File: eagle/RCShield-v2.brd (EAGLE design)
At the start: 92.7 x 82.5 mm, 48 parts, among them J1/J2 JOYSTICKPTH, U1 TOUSCRUINO_SHIELD, U2 FT232RL-BASICSSOP, U4 XBEE, X1 USBSMD

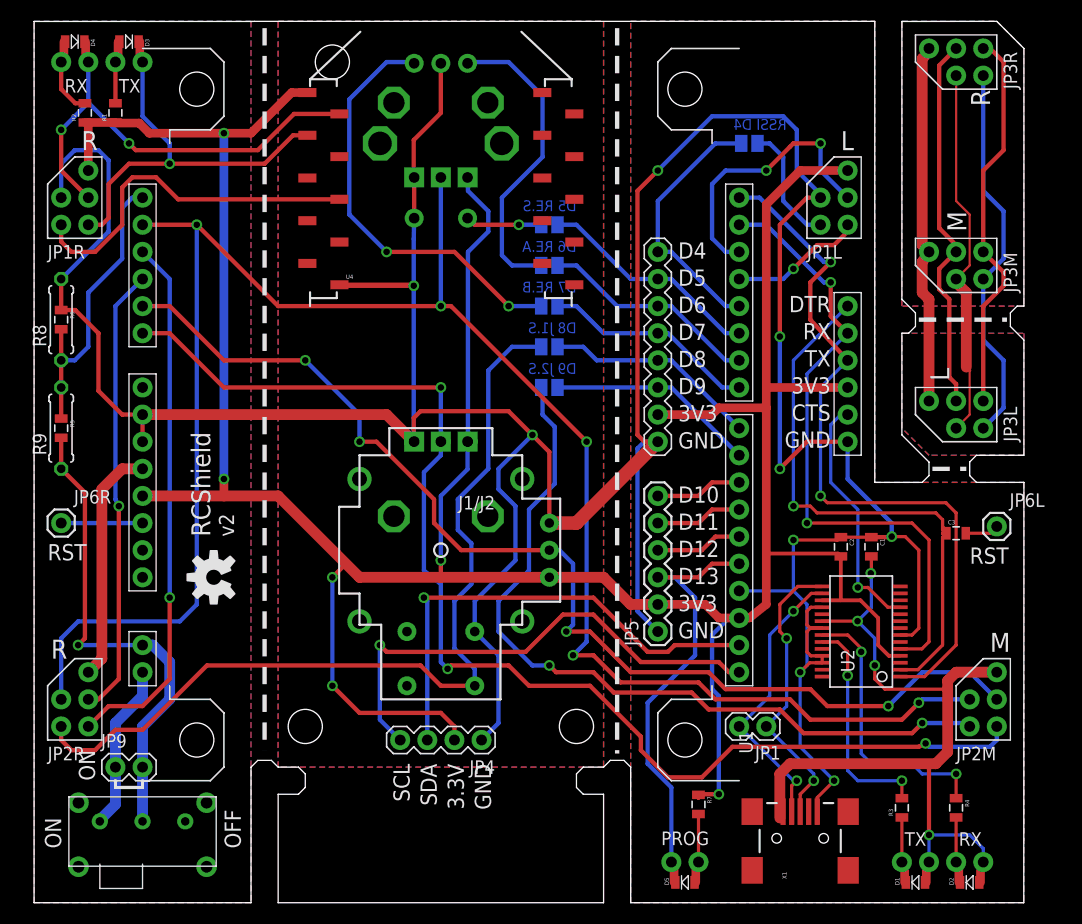
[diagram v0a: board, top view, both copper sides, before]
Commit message: 
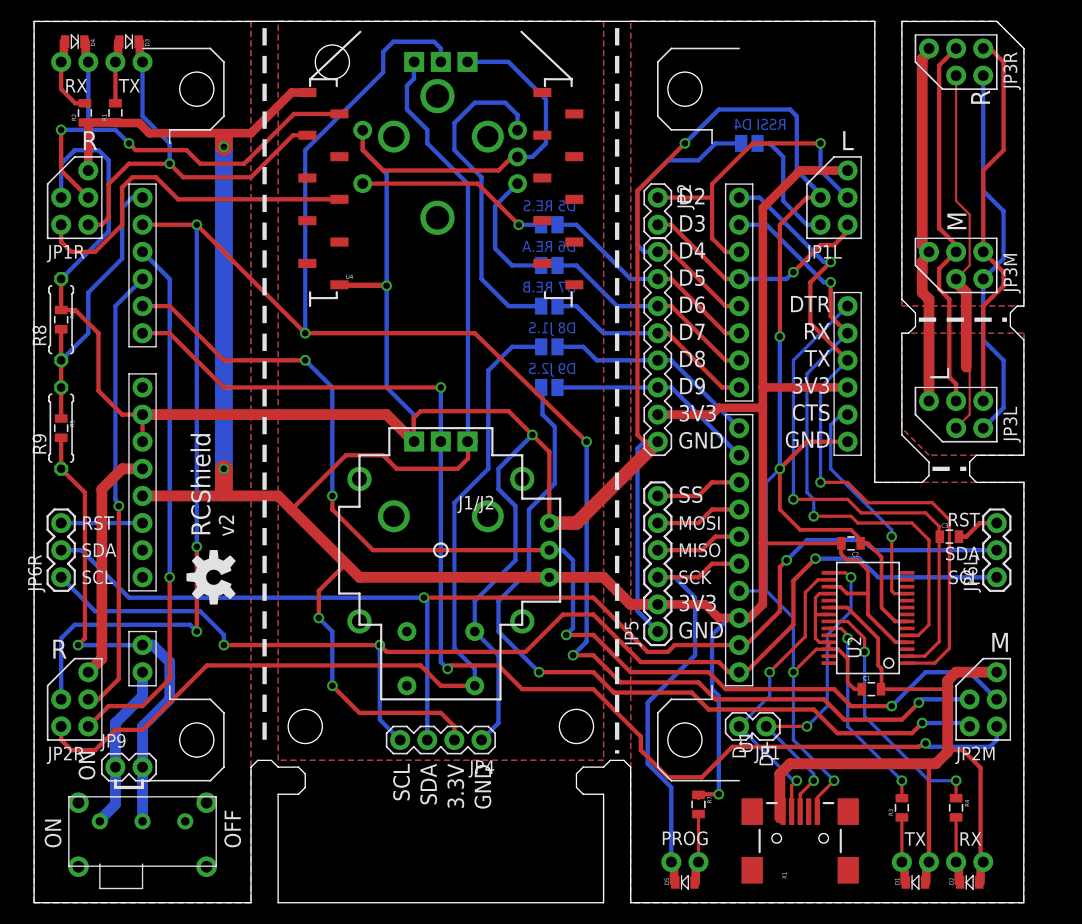
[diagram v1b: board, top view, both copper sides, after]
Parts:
- added JP2: UART1, wibauxl:1X02
- JP6L, JP6R: device SparkFun:1X01 -> SparkFun:1X03
- P1/P3, P2/P4: value (none) -> POT; device SparkFun:ALPS_POT -> wibauxl:ALPS_POT
- moved C1 13.3 mm to (78.4, 20.0), turned to 0 degrees
- moved JP6R 5.08 mm to (2.54, 30.5), turned to 90 degrees
- moved JP6L 4.76 mm to (90.2, 30.5), turned to 90 degrees
- moved P2/P4 3.18 mm to (38.1, 71.8), turned to 90 degrees
- moved U2 1.42 mm to (78.1, 26.7)
- moved RE1 1.31 mm to (37.8, 69.8), turned to 90 degrees
- moved C2 1.00 mm to (76.5, 33.7), turned to 180 degrees
- moved C3 0.71 mm to (85.7, 34.3)
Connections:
- removed net N$11: C3.2, JP6L.1
- new net N$1: C3.2, JP6L.3
- net RES: now also JP6R.3; no longer JP6R.1
- net RX1: now also JP2.1
- net SCL: now also JP6L.1, JP6R.1
- net SDA: now also JP6L.2, JP6R.2
- net TX1: now also JP2.2
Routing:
- net SDA: track 45.4 -> 112.1 mm, vias 1 -> 2
- net SCL: track 47.3 -> 112.0 mm, vias 1 -> 3
- net 3.3V: track 303.4 -> 334.8 mm, vias 6 -> 5
- net A4: track 178.3 -> 204.9 mm, vias 5 -> 7
- net GND: track 375.6 -> 401.7 mm, vias 9 -> 7
- net RE.A: track 29.0 -> 11.9 mm
- net RE.S: track 7.14 -> 18.3 mm
- net TX1: track 12.6 -> 22.4 mm
- net RE.B: track 39.9 -> 30.9 mm, vias 2 -> 0
- net RX1: track 26.0 -> 31.1 mm, vias 2 -> 1
- net D+: track 27.5 -> 32.0 mm, vias 2 -> 3
- net A1: track 105.3 -> 109.6 mm
- net N$1: track 0.00 -> 4.07 mm
- net U_DTR: track 53.4 -> 49.3 mm
- net D4: track 24.5 -> 28.5 mm
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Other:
- board text added: "D+"
- board text added: "D-"
- board text added: "D2"
- board text added: "D3"
- board text added: "MISO"
- board text added: "MOSI"
- board text added: "SCK"
- board text added: "SS"
- board text removed: "D10"
- board text removed: "D11"
- board text removed: "D12"
- board text removed: "D13"

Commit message: 
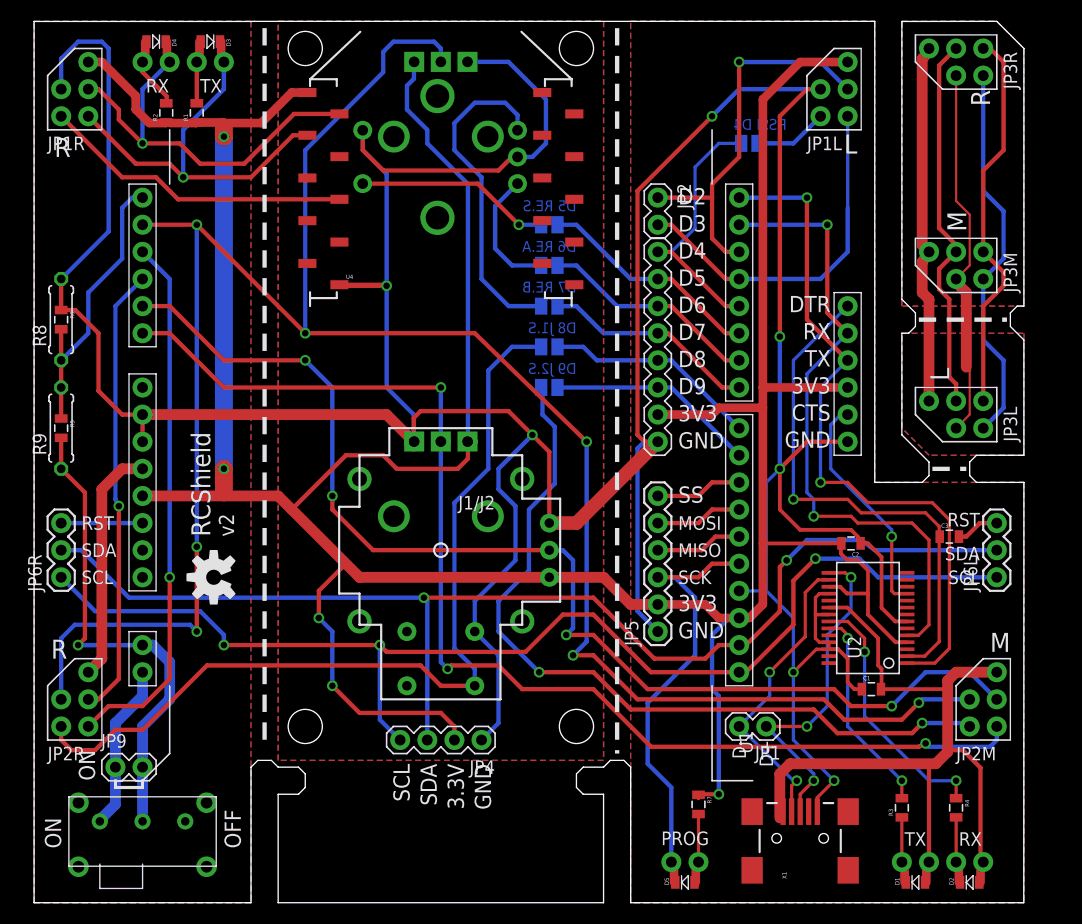
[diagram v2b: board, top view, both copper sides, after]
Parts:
- moved JP1L 10.2 mm to (73.7, 74.9)
- moved JP1R 10.2 mm to (2.54, 74.9)
- moved D3 7.62 mm to (16.5, 80.6)
- moved R1 7.62 mm to (15.2, 74.0)
- moved R2 7.62 mm to (12.4, 74.0)
- moved D4 7.62 mm to (11.4, 80.6)
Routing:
- net GND: track 401.7 -> 415.9 mm
- net TX1: track 22.4 -> 33.6 mm, vias 1 -> 0
- net 3.3V: track 334.8 -> 344.0 mm
- net RX1: track 31.1 -> 36.9 mm
- net X_TX: track 43.1 -> 37.6 mm, vias 2 -> 1
- net RSSI: track 33.8 -> 29.3 mm
- net _RSSI: track 11.5 -> 6.96 mm
- net D4: track 28.5 -> 25.1 mm
- net A0: track 116.2 -> 113.1 mm
- net U_RX: track 57.3 -> 60.3 mm
- net U_TX: track 65.1 -> 65.8 mm
- net X_RX: track 37.5 -> 36.9 mm
- net SDA: track 112.1 -> 112.6 mm
- net N$25: track 5.31 -> 4.81 mm

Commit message: 
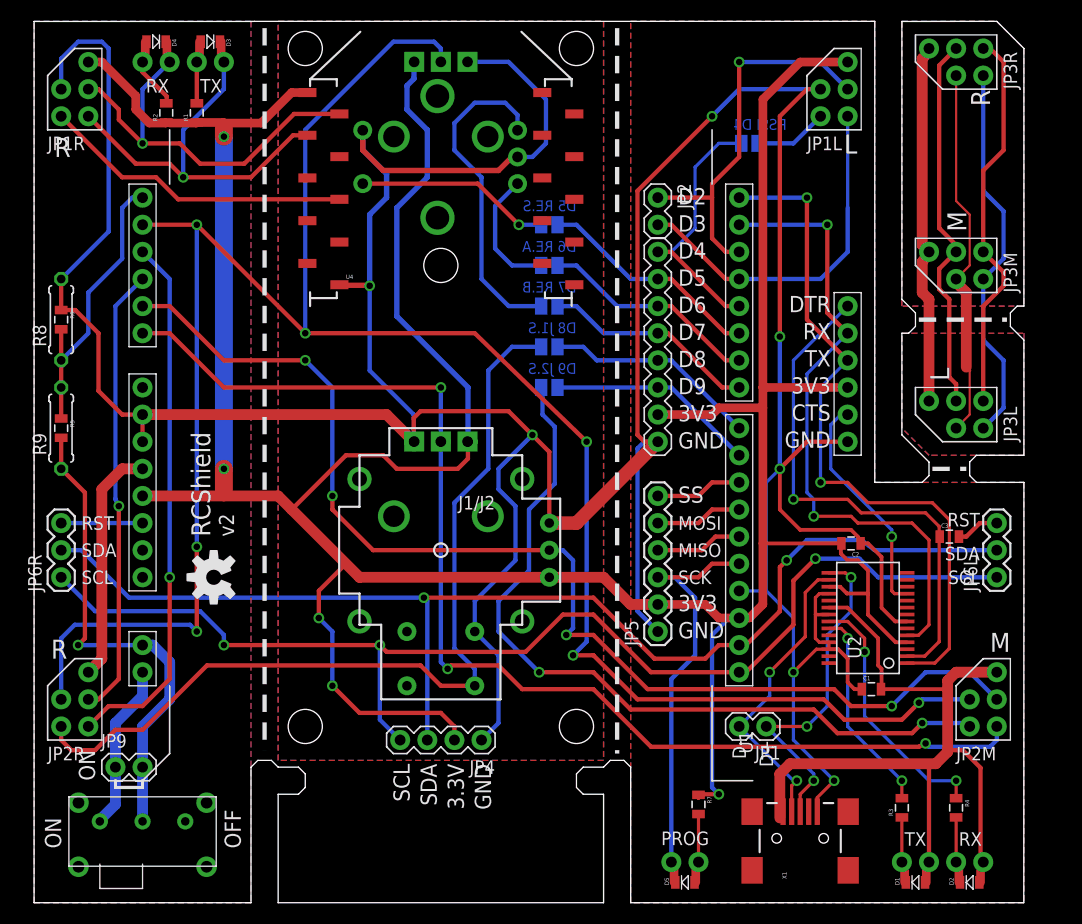
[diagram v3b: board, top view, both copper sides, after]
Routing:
- net 3.3V: track 344.0 -> 346.4 mm
- net GND: track 415.9 -> 414.0 mm
- net SCK: track 40.0 -> 38.1 mm
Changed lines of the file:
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@@
 <grid distance="12.5" unitdist="mil" unit="mil" style="lines" multiple="8" display="yes" altdistance="6.25" altunitdist="mil" altunit="mil"/>
 <layers>
-<layer number="1" name="Top" color="4" fill="1" visible="no" active="yes"/>
+<layer number="1" name="Top" color="4" fill="1" visible="yes" active="yes"/>
 <layer number="16" name="Bottom" color="1" fill="1" visible="yes" active="yes"/>
 <layer number="17" name="Pads" color="2" fill="1" visible="yes" active="yes"/>
@@
 <text x="60.325" y="65.405" size="1.524" layer="21" font="vector" ratio="15">D2</text>
 <hole x="50.8" y="80.01" drill="3.2"/>
+<hole x="38.1" y="59.69" drill="3.2"/>
 </plain>
 <attributes>
@@
 <wire x1="48.26" y1="35.56" x2="50.8" y2="35.56" width="1.27" layer="1"/>
 <wire x1="50.8" y1="35.56" x2="58.42" y2="43.18" width="1.27" layer="1"/>
-<wire x1="33.02" y1="57.785" x2="28.695" y2="57.785" width="0.4064" layer="1"/>
+<wire x1="31.4325" y1="57.785" x2="28.695" y2="57.785" width="0.4064" layer="1"/>
 <wire x1="28.695" y1="57.785" x2="28.6" y2="57.88" width="0.4064" layer="1"/>
 <wire x1="2.54" y1="76.2" x2="2.54" y2="79.0575" width="0.4064" layer="16"/>
@@
 <wire x1="6.985" y1="62.865" x2="2.54" y2="58.42" width="0.4064" layer="16"/>
 <wire x1="2.54" y1="55.51" x2="2.54" y2="58.42" width="0.4064" layer="1"/>
-<wire x1="28.6" y1="57.88" x2="32.925" y2="57.88" width="0.4064" layer="1"/>
-<wire x1="32.925" y1="57.88" x2="33.02" y2="57.785" width="0.4064" layer="1"/>
-<wire x1="33.02" y1="57.785" x2="33.02" y2="48.26" width="0.4064" layer="16"/>
+<wire x1="28.6" y1="57.88" x2="31.3375" y2="57.88" width="0.4064" layer="1"/>
+<wire x1="31.3375" y1="57.88" x2="31.4325" y2="57.785" width="0.4064" layer="1"/>
+<wire x1="31.4325" y1="57.785" x2="31.4325" y2="49.8475" width="0.4064" layer="16"/>
+<wire x1="31.4325" y1="49.8475" x2="33.02" y2="48.26" width="0.4064" layer="16"/>
 <wire x1="33.02" y1="48.26" x2="35.56" y2="45.72" width="0.4064" layer="16"/>
 <wire x1="35.56" y1="45.72" x2="35.56" y2="43.18" width="0.4064" layer="16"/>
-<via x="33.02" y="57.785" extent="1-16" drill="0.6096"/>
+<via x="31.4325" y="57.785" extent="1-16" drill="0.6096"/>
 <wire x1="35.56" y1="43.18" x2="33.02" y2="45.72" width="1.016" layer="1"/>
 <wire x1="33.02" y1="45.72" x2="10.16" y2="45.72" width="1.016" layer="1"/>
@@
 <vertex x="22.86" y="13.335"/>
 </polygon>
-<wire x1="30.7825" y1="72.35" x2="30.7825" y2="70.5" width="0.4064" layer="16"/>
-<wire x1="30.7825" y1="70.5" x2="33.02" y2="68.2625" width="0.4064" layer="16"/>
-<wire x1="33.02" y1="68.2625" x2="33.02" y2="57.785" width="0.4064" layer="16"/>
+<wire x1="30.7825" y1="72.35" x2="30.7825" y2="70.5" width="0.508" layer="16"/>
+<wire x1="30.7825" y1="70.5" x2="33.02" y2="68.2625" width="0.508" layer="16"/>
+<wire x1="33.02" y1="68.2625" x2="33.02" y2="66.04" width="0.508" layer="16"/>
+<wire x1="33.02" y1="66.04" x2="31.4325" y2="64.4525" width="0.508" layer="16"/>
+<wire x1="31.4325" y1="64.4525" x2="31.4325" y2="57.785" width="0.508" layer="16"/>
 <wire x1="45.2825" y1="69.85" x2="44.7675" y2="69.85" width="0.4064" layer="1"/>
-<wire x1="44.7675" y1="69.85" x2="43.4975" y2="68.58" width="0.4064" layer="1"/>
-<wire x1="43.4975" y1="68.58" x2="32.7025" y2="68.58" width="0.4064" layer="1"/>
-<wire x1="32.7025" y1="68.58" x2="30.7825" y2="70.5" width="0.4064" layer="1"/>
-<wire x1="30.7825" y1="70.5" x2="30.7825" y2="72.35" width="0.4064" layer="1"/>
+<wire x1="44.7675" y1="69.85" x2="43.4975" y2="68.58" width="0.508" layer="1"/>
+<wire x1="43.4975" y1="68.58" x2="32.7025" y2="68.58" width="0.508" layer="1"/>
+<wire x1="32.7025" y1="68.58" x2="30.7825" y2="70.5" width="0.508" layer="1"/>
+<wire x1="30.7825" y1="70.5" x2="30.7825" y2="72.35" width="0.508" layer="1"/>
 <wire x1="40.6" y1="78.755" x2="44.435" y2="78.755" width="0.4064" layer="16"/>
 <wire x1="44.435" y1="78.755" x2="47.9425" y2="75.2475" width="0.4064" layer="16"/>
@@
 <wire x1="66.04" y1="26.67" x2="65.0875" y2="26.67" width="0.4064" layer="16"/>
 <wire x1="65.0875" y1="26.67" x2="63.5" y2="25.0825" width="0.4064" layer="16"/>
-<wire x1="63.5" y1="25.0825" x2="63.5" y2="20.0025" width="0.4064" layer="16"/>
-<wire x1="63.5" y1="20.0025" x2="64.135" y2="19.3675" width="0.4064" layer="16"/>
-<wire x1="64.135" y1="19.3675" x2="64.135" y2="10.16" width="0.4064" layer="16"/>
+<wire x1="63.5" y1="25.0825" x2="63.5" y2="10.795" width="0.4064" layer="16"/>
+<wire x1="63.5" y1="10.795" x2="64.135" y2="10.16" width="0.4064" layer="16"/>
 <wire x1="64.135" y1="10.16" x2="62.5475" y2="10.16" width="0.4064" layer="1"/>
 <via x="64.135" y="10.16" extent="1-16" drill="0.6096"/>
@@
 <wire x1="17.78" y1="38.57625" x2="17.78" y2="38.1" width="0.3048" layer="1"/>
 <wire x1="17.78" y1="40.64" x2="17.78" y2="38.57625" width="1.6764" layer="1"/>
-<wire x1="35.6" y1="78.755" x2="35.575" y2="77.1675" width="0.4064" layer="16"/>
-<wire x1="35.575" y1="77.1675" x2="34.925" y2="76.5175" width="0.4064" layer="16"/>
-<wire x1="34.925" y1="76.5175" x2="34.925" y2="74.295" width="0.4064" layer="16"/>
-<wire x1="34.925" y1="74.295" x2="36.83" y2="72.39" width="0.4064" layer="16"/>
-<wire x1="36.83" y1="72.39" x2="36.83" y2="71.12" width="0.4064" layer="16"/>
-<wire x1="36.83" y1="71.12" x2="40.64" y2="67.31" width="0.4064" layer="16"/>
-<wire x1="40.64" y1="67.31" x2="40.64" y2="43.18" width="0.4064" layer="16"/>
+<wire x1="35.6" y1="78.755" x2="35.575" y2="77.1675" width="0.508" layer="16"/>
+<wire x1="35.575" y1="77.1675" x2="34.925" y2="76.5175" width="0.508" layer="16"/>
+<wire x1="34.925" y1="76.5175" x2="34.925" y2="74.295" width="0.508" layer="16"/>
+<wire x1="34.925" y1="74.295" x2="36.83" y2="72.39" width="0.508" layer="16"/>
+<wire x1="36.83" y1="72.39" x2="36.83" y2="67.945" width="0.508" layer="16"/>
+<wire x1="36.83" y1="67.945" x2="33.9725" y2="65.0875" width="0.508" layer="16"/>
+<wire x1="33.9725" y1="65.0875" x2="33.9725" y2="54.9275" width="0.508" layer="16"/>
+<wire x1="33.9725" y1="54.9275" x2="40.64" y2="48.26" width="0.508" layer="16"/>
+<wire x1="40.64" y1="48.26" x2="40.64" y2="43.18" width="0.508" layer="16"/>
 <wire x1="9.525" y1="74.295" x2="10.795" y2="73.025" width="0.8128" layer="1"/>
 <wire x1="10.795" y1="73.025" x2="12.33" y2="73.025" width="0.8128" layer="1"/>
@@
 <wire x1="38.1" y1="80.01" x2="37.465" y2="80.645" width="0.4064" layer="16"/>
 <wire x1="37.465" y1="80.645" x2="33.655" y2="80.645" width="0.4064" layer="16"/>
-<wire x1="33.655" y1="80.645" x2="32.7025" y2="79.6925" width="0.4064" layer="16"/>
-<wire x1="32.7025" y1="79.6925" x2="32.7025" y2="77.7875" width="0.4064" layer="16"/>
-<wire x1="32.7025" y1="77.7875" x2="25.4" y2="70.485" width="0.4064" layer="16"/>
-<wire x1="25.4" y1="70.485" x2="25.4" y2="53.34" width="0.4064" layer="16"/>
+<wire x1="33.655" y1="80.645" x2="25.4" y2="72.39" width="0.4064" layer="16"/>
+<wire x1="25.4" y1="72.39" x2="25.4" y2="53.34" width="0.4064" layer="16"/>
 </signal>
 <signal name="A5">
@@
 <wire x1="60.0075" y1="30.48" x2="61.9125" y2="28.575" width="0.4064" layer="16"/>
 <wire x1="61.9125" y1="28.575" x2="61.9125" y2="23.1775" width="0.4064" layer="16"/>
-<wire x1="61.9125" y1="23.1775" x2="57.4675" y2="18.7325" width="0.4064" layer="16"/>
-<wire x1="57.4675" y1="18.7325" x2="57.4675" y2="13.0175" width="0.4064" layer="16"/>
-<wire x1="57.4675" y1="13.0175" x2="59.69" y2="10.795" width="0.4064" layer="16"/>
-<wire x1="59.69" y1="10.795" x2="59.69" y2="3.81" width="0.4064" layer="16"/>
+<wire x1="61.9125" y1="23.1775" x2="59.69" y2="20.955" width="0.4064" layer="16"/>
+<wire x1="59.69" y1="20.955" x2="59.69" y2="3.81" width="0.4064" layer="16"/>
 </signal>
 <signal name="J1.S">
@@
 </signal>
 </signals>
-<errors>
-</errors>
 </board>
 </drawing>

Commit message: 
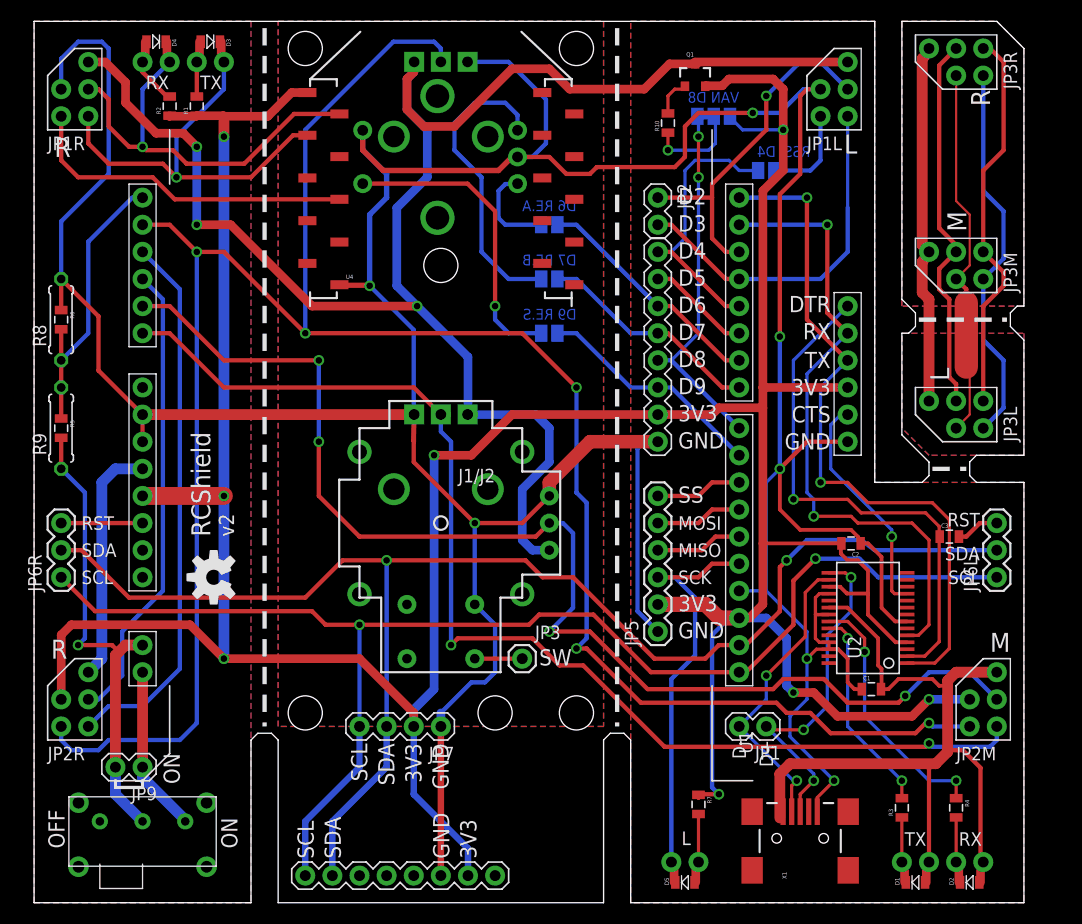
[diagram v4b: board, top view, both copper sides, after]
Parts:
- removed SJ1: (no value), jumper:SJ
- added JP3: (no value), SparkFun:1X01
- added JP7: (no value), wibauxl:1X04
- added Q1: MMBT3906, wibauxl:SOT23-3
- added R10: 10K, SparkFun:0805
- JP4: value I2C -> (none); device wibauxl:1X04 -> wibauxl:1X08
- SJ2: device jumper:SJ -> wibauxl:SJ_2WAYS_1-2
- moved SJ2 29.7 mm to (63.7, 73.7), turned to 180 degrees
- moved JP4 12.8 mm to (43.2, 2.54)
- moved SJ5 10.2 mm to (48.3, 53.3)
- moved SJ4 3.81 mm to (48.3, 63.5)
- moved SJ6 3.00 mm to (68.6, 68.6)
- moved JP9 2.54 mm to (10.2, 12.7), turned to 180 degrees
- moved J1/J2 2.54 mm to (38.1, 35.6)
- moved P1/P3 2.54 mm to (38.1, 38.7)
- moved SJ3 2.54 mm to (48.3, 58.4)
- moved R2 0.71 mm to (12.7, 74.6)
- moved R1 0.63 mm to (15.2, 74.6)
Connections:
- removed net J2.S: JP2M.2, SJ2.2
- new net N$2: Q1.1, R10.2
- new net N$3: R10.1, SJ2.2
- new net VAN: J1/J2.H1, J1/J2.V1, JP1L.5, JP1R.5, P1/P3.P$1, P2/P4.P$3, Q1.3
- net 3.3V: now also JP2M.1, JP2R.1, JP7.2, Q1.2, SJ2.3; no longer J1/J2.H1, J1/J2.V1, JP1L.5, JP1R.5, P1/P3.P$1, P2/P4.P$3
- net A4: now also JP2M.2, JP2R.2; no longer JP2M.1, JP2R.1
- net D5: no longer SJ5.2
- net D8: now also SJ2.1; no longer SJ1.1
- net D9: now also SJ5.2; no longer SJ2.1
- net GND: now also JP4.3, JP7.1; no longer JP4.1
- net J1.S: now also JP3.1; no longer JP2R.2, SJ1.2
- net SCL: now also JP4.8, JP7.4; no longer JP4.4
- net SDA: now also JP4.7, JP7.3; no longer JP4.3
- net VBAT: now also S4.3; no longer S4.1
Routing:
- net VAN: track 0.00 -> 158.6 mm, vias 0 -> 3
- net J1.S: track 82.0 -> 4.45 mm
- net J2.S: track 74.2 -> 0.00 mm, vias 2 -> 0
- net SDA: track 112.6 -> 133.7 mm
- net D8: track 20.2 -> 34.2 mm, vias 0 -> 2
- net SCL: track 112.0 -> 125.2 mm, vias 3 -> 2
- net D5: track 21.2 -> 9.72 mm
- net GND: track 414.0 -> 403.6 mm
- net RE.S: track 18.3 -> 28.5 mm
- net N$3: track 0.00 -> 9.05 mm, vias 0 -> 1
- net A1: track 109.6 -> 115.5 mm
- net A4: track 204.9 -> 209.1 mm, vias 7 -> 5
- net N$2: track 0.00 -> 3.60 mm
- net RX1: track 36.9 -> 33.6 mm
- net RE.A: track 11.9 -> 8.85 mm
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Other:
- outline, holes or cut-outs redrawn
- board text added: "D9 RE.S"
- board text added: "SW"
- board text added: "VAN D8"
- board text removed: "3.3V"
- board text removed: "D5 RE.S"
- board text removed: "D8 J1.S"
- board text removed: "D9 J2.S"
- board text removed: "PROG"
